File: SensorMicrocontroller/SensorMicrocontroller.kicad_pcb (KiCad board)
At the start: 2 copper layers, 100 x 100 mm, 36 parts, among them J1 JST B4B-PH-SM4-TB, J2 JST B4B-PH-SM4-TB, J3 JST B6B-PH-SM4-TB, J4 JST B4B-PH-SM4-TB, J5 JST B4B-PH-SM4-TB, J8 12V Connector, J9 Light Connector, Q1 DMT6009LCT, Q2 DMT6009LCT, U1 ADS1115IDGS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

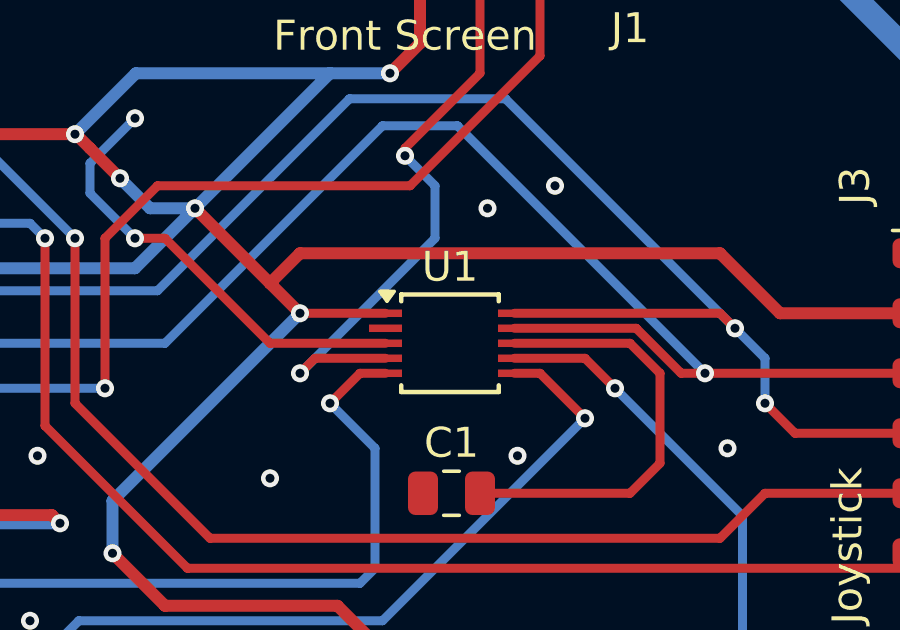
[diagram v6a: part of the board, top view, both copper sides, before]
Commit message: Fixed ADS1115 footprint
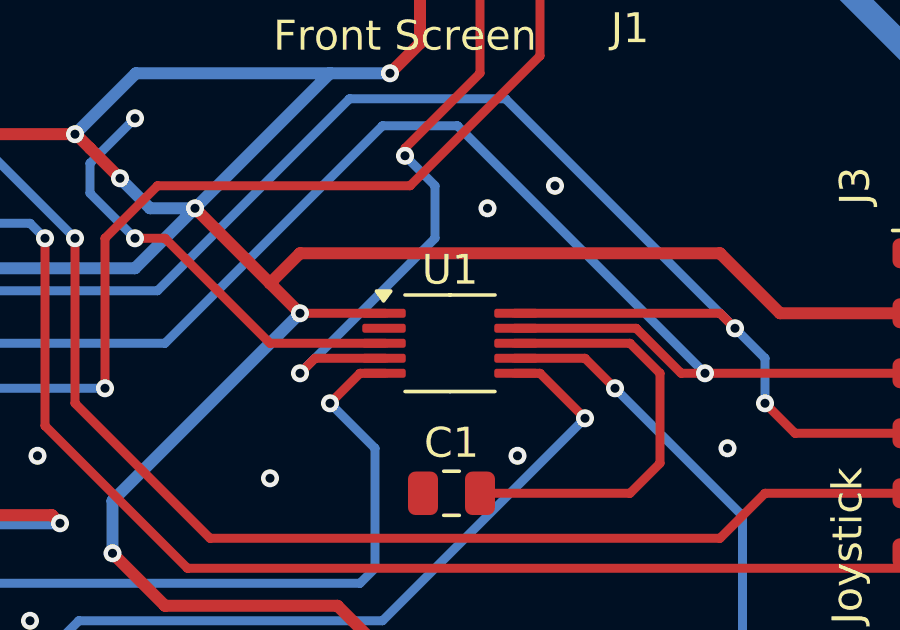
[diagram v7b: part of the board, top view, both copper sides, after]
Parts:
- U1: footprint Package_SO:TSSOP-10_3x3mm_P0.5mm -> Package_SO:VSSOP-10_3x3mm_P0.5mm
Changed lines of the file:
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@@
 		)
 	)
-	(footprint "Package_SO:TSSOP-10_3x3mm_P0.5mm"
+	(footprint "Package_SO:VSSOP-10_3x3mm_P0.5mm"
 		(layer "F.Cu")
 		(at 172 68)
-		(descr "TSSOP10: plastic thin shrink small outline package; 10 leads; body width 3 mm; (see NXP SSOP-TSSOP-VSO-REFLOW.pdf and sot552-1_po.pdf)")
-		(tags "SSOP 0.5")
+		(descr "VSSOP, 10 Pin (http://www.ti.com/lit/ds/symlink/ads1115.pdf), generated with kicad-footprint-generator ipc_gullwing_generator.py")
+		(tags "VSSOP SO")
 		(property "Reference" "U1"
-			(at 0 -2.55 0)
+			(at 0 -2.45 0)
 			(layer "F.SilkS")
 			(effects
@@
 		)
 		(property "Value" "ADS1115IDGS"
-			(at 0 2.55 0)
+			(at 0 2.45 0)
 			(layer "F.Fab")
 			(effects
@@
 			)
 		)
-		(property "Footprint" "Package_SO:TSSOP-10_3x3mm_P0.5mm"
-			(at 0 0 0)
-			(unlocked yes)
+		(property "Footprint" "Package_SO:VSSOP-10_3x3mm_P0.5mm"
+			(at 0 0 0)
 			(layer "F.Fab")
 			(hide yes)
@@
 		(property "Datasheet" "http://www.ti.com/lit/ds/symlink/ads1113.pdf"
 			(at 0 0 0)
-			(unlocked yes)
 			(layer "F.Fab")
 			(hide yes)
@@
 		(property "Description" "Ultra-Small, Low-Power, I2C-Compatible, 860-SPS, 16-Bit ADCs With Internal Reference, Oscillator, and Programmable Comparator, VSSOP-10"
 			(at 0 0 0)
-			(unlocked yes)
 			(layer "F.Fab")
 			(hide yes)
@@
 		(attr smd)
 		(fp_line
-			(start -1.625 -1.625)
-			(end -1.625 -1.4)
-			(stroke
-				(width 0.15)
-				(type solid)
-			)
-			(layer "F.SilkS")
-		)
-		(fp_line
-			(start -1.625 -1.625)
-			(end 1.625 -1.625)
-			(stroke
-				(width 0.15)
-				(type solid)
-			)
-			(layer "F.SilkS")
-		)
-		(fp_line
-			(start -1.625 1.625)
-			(end -1.625 1.4)
-			(stroke
-				(width 0.15)
-				(type solid)
-			)
-			(layer "F.SilkS")
-		)
-		(fp_line
-			(start -1.625 1.625)
-			(end 1.625 1.625)
-			(stroke
-				(width 0.15)
-				(type solid)
-			)
-			(layer "F.SilkS")
-		)
-		(fp_line
-			(start 1.625 -1.625)
-			(end 1.625 -1.4)
-			(stroke
-				(width 0.15)
-				(type solid)
-			)
-			(layer "F.SilkS")
-		)
-		(fp_line
-			(start 1.625 1.625)
-			(end 1.625 1.4)
-			(stroke
-				(width 0.15)
+			(start 0 -1.61)
+			(end -1.5 -1.61)
+			(stroke
+				(width 0.12)
+				(type solid)
+			)
+			(layer "F.SilkS")
+		)
+		(fp_line
+			(start 0 -1.61)
+			(end 1.5 -1.61)
+			(stroke
+				(width 0.12)
+				(type solid)
+			)
+			(layer "F.SilkS")
+		)
+		(fp_line
+			(start 0 1.61)
+			(end -1.5 1.61)
+			(stroke
+				(width 0.12)
+				(type solid)
+			)
+			(layer "F.SilkS")
+		)
+		(fp_line
+			(start 0 1.61)
+			(end 1.5 1.61)
+			(stroke
+				(width 0.12)
 				(type solid)
 			)
@@
 		(fp_poly
 			(pts
-				(xy -2.1 -1.4) (xy -2.34 -1.73) (xy -1.86 -1.73) (xy -2.1 -1.4)
+				(xy -2.2125 -1.41) (xy -2.4525 -1.74) (xy -1.9725 -1.74) (xy -2.2125 -1.41)
 			)
 			(stroke
@@
 		)
 		(fp_line
-			(start -2.95 -1.8)
-			(end -2.95 1.8)
+			(start -3.18 -1.75)
+			(end -3.18 1.75)
 			(stroke
 				(width 0.05)
@@
 		)
 		(fp_line
-			(start -2.95 -1.8)
-			(end 2.95 -1.8)
+			(start -3.18 1.75)
+			(end 3.18 1.75)
 			(stroke
 				(width 0.05)
@@
 		)
 		(fp_line
-			(start -2.95 1.8)
-			(end 2.95 1.8)
+			(start 3.18 -1.75)
+			(end -3.18 -1.75)
 			(stroke
 				(width 0.05)
@@
 		)
 		(fp_line
-			(start 2.95 -1.8)
-			(end 2.95 1.8)
+			(start 3.18 1.75)
+			(end 3.18 -1.75)
 			(stroke
 				(width 0.05)
@@
 		)
 		(fp_line
-			(start -1.5 -0.5)
-			(end -0.5 -1.5)
+			(start -1.5 -0.75)
+			(end -0.75 -1.5)
 			(stroke
 				(width 0.1)
@@
 		(fp_line
 			(start -1.5 1.5)
-			(end -1.5 -0.5)
-			(stroke
-				(width 0.1)
-				(type solid)
-			)
-			(layer "F.Fab")
-		)
-		(fp_line
-			(start -0.5 -1.5)
+			(end -1.5 -0.75)
+			(stroke
+				(width 0.1)
+				(type solid)
+			)
+			(layer "F.Fab")
+		)
+		(fp_line
+			(start -0.75 -1.5)
 			(end 1.5 -1.5)
 			(stroke
@@
 			(effects
 				(font
-					(size 0.6 0.6)
-					(thickness 0.1)
-				)
-			)
-		)
-		(pad "1" smd rect
-			(at -2.15 -1)
-			(size 1.1 0.25)
-			(layers "F.Cu" "F.Paste" "F.Mask")
+					(size 0.75 0.75)
+					(thickness 0.11)
+				)
+			)
+		)
+		(pad "1" smd roundrect
+			(at -2.2 -1)
+			(size 1.45 0.3)
+			(layers "F.Cu" "F.Paste" "F.Mask")
+			(roundrect_rratio 0.25)
 			(net 7 "/3.3V")
 			(pinfunction "ADDR")
 			(pintype "input")
 		)
-		(pad "2" smd rect
-			(at -2.15 -0.5)
-			(size 1.1 0.25)
-			(layers "F.Cu" "F.Paste" "F.Mask")
+		(pad "2" smd roundrect
+			(at -2.2 -0.5)
+			(size 1.45 0.3)
+			(layers "F.Cu" "F.Paste" "F.Mask")
+			(roundrect_rratio 0.25)
 			(net 29 "unconnected-(U1-ALERT{slash}RDY-Pad2)")
 			(pinfunction "ALERT/RDY")
 			(pintype "output")
 		)
-		(pad "3" smd rect
-			(at -2.15 0)
-			(size 1.1 0.25)
-			(layers "F.Cu" "F.Paste" "F.Mask")
+		(pad "3" smd roundrect
+			(at -2.2 0)
+			(size 1.45 0.3)
+			(layers "F.Cu" "F.Paste" "F.Mask")
+			(roundrect_rratio 0.25)
 			(net 2 "/GND")
 			(pinfunction "GND")
 			(pintype "power_in")
 		)
-		(pad "4" smd rect
-			(at -2.15 0.5)
-			(size 1.1 0.25)
-			(layers "F.Cu" "F.Paste" "F.Mask")
+		(pad "4" smd roundrect
+			(at -2.2 0.5)
+			(size 1.45 0.3)
+			(layers "F.Cu" "F.Paste" "F.Mask")
+			(roundrect_rratio 0.25)
 			(net 9 "/US0")
 			(pinfunction "AIN0")
 			(pintype "input")
 		)
-		(pad "5" smd rect
-			(at -2.15 1)
-			(size 1.1 0.25)
-			(layers "F.Cu" "F.Paste" "F.Mask")
+		(pad "5" smd roundrect
+			(at -2.2 1)
+			(size 1.45 0.3)
+			(layers "F.Cu" "F.Paste" "F.Mask")
+			(roundrect_rratio 0.25)
 			(net 11 "/US1")
 			(pinfunction "AIN1")
 			(pintype "input")
 		)
-		(pad "6" smd rect
-			(at 2.15 1)
-			(size 1.1 0.25)
-			(layers "F.Cu" "F.Paste" "F.Mask")
+		(pad "6" smd roundrect
+			(at 2.2 1)
+			(size 1.45 0.3)
+			(layers "F.Cu" "F.Paste" "F.Mask")
+			(roundrect_rratio 0.25)
 			(net 12 "/US2")
 			(pinfunction "AIN2")
 			(pintype "input")
 		)
-		(pad "7" smd rect
-			(at 2.15 0.5)
-			(size 1.1 0.25)
-			(layers "F.Cu" "F.Paste" "F.Mask")
+		(pad "7" smd roundrect
+			(at 2.2 0.5)
+			(size 1.45 0.3)
+			(layers "F.Cu" "F.Paste" "F.Mask")
+			(roundrect_rratio 0.25)
 			(net 14 "/US3")
 			(pinfunction "AIN3")
 			(pintype "input")
 		)
-		(pad "8" smd rect
-			(at 2.15 0)
-			(size 1.1 0.25)
-			(layers "F.Cu" "F.Paste" "F.Mask")
+		(pad "8" smd roundrect
+			(at 2.2 0)
+			(size 1.45 0.3)
+			(layers "F.Cu" "F.Paste" "F.Mask")
+			(roundrect_rratio 0.25)
 			(net 1 "Net-(U1-VDD)")
 			(pinfunction "VDD")
 			(pintype "power_in")
 		)
-		(pad "9" smd rect
-			(at 2.15 -0.5)
-			(size 1.1 0.25)
-			(layers "F.Cu" "F.Paste" "F.Mask")
+		(pad "9" smd roundrect
+			(at 2.2 -0.5)
+			(size 1.45 0.3)
+			(layers "F.Cu" "F.Paste" "F.Mask")
+			(roundrect_rratio 0.25)
 			(net 6 "/SDA")
 			(pinfunction "SDA")
 			(pintype "bidirectional")
 		)
-		(pad "10" smd rect
-			(at 2.15 -1)
-			(size 1.1 0.25)
-			(layers "F.Cu" "F.Paste" "F.Mask")
+		(pad "10" smd roundrect
+			(at 2.2 -1)
+			(size 1.45 0.3)
+			(layers "F.Cu" "F.Paste" "F.Mask")
+			(roundrect_rratio 0.25)
 			(net 4 "/SCL")
 			(pinfunction "SCL")
 			(pintype "input")
 		)
-		(model "${KICAD8_3DMODEL_DIR}/Package_SO.3dshapes/TSSOP-10_3x3mm_P0.5mm.wrl"
+		(model "${KICAD8_3DMODEL_DIR}/Package_SO.3dshapes/VSSOP-10_3x3mm_P0.5mm.wrl"
 			(offset
 				(xyz 0 0 0)

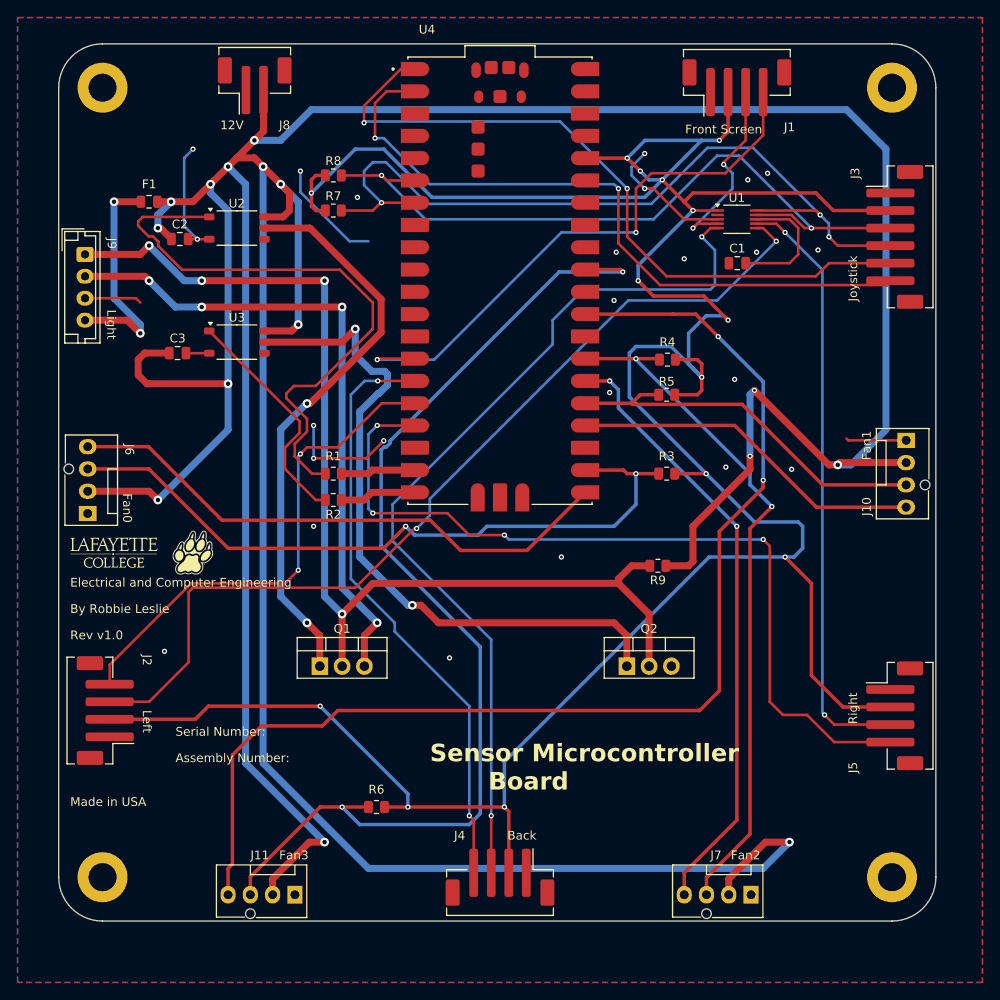
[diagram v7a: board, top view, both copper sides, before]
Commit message: Added cap for fan tach
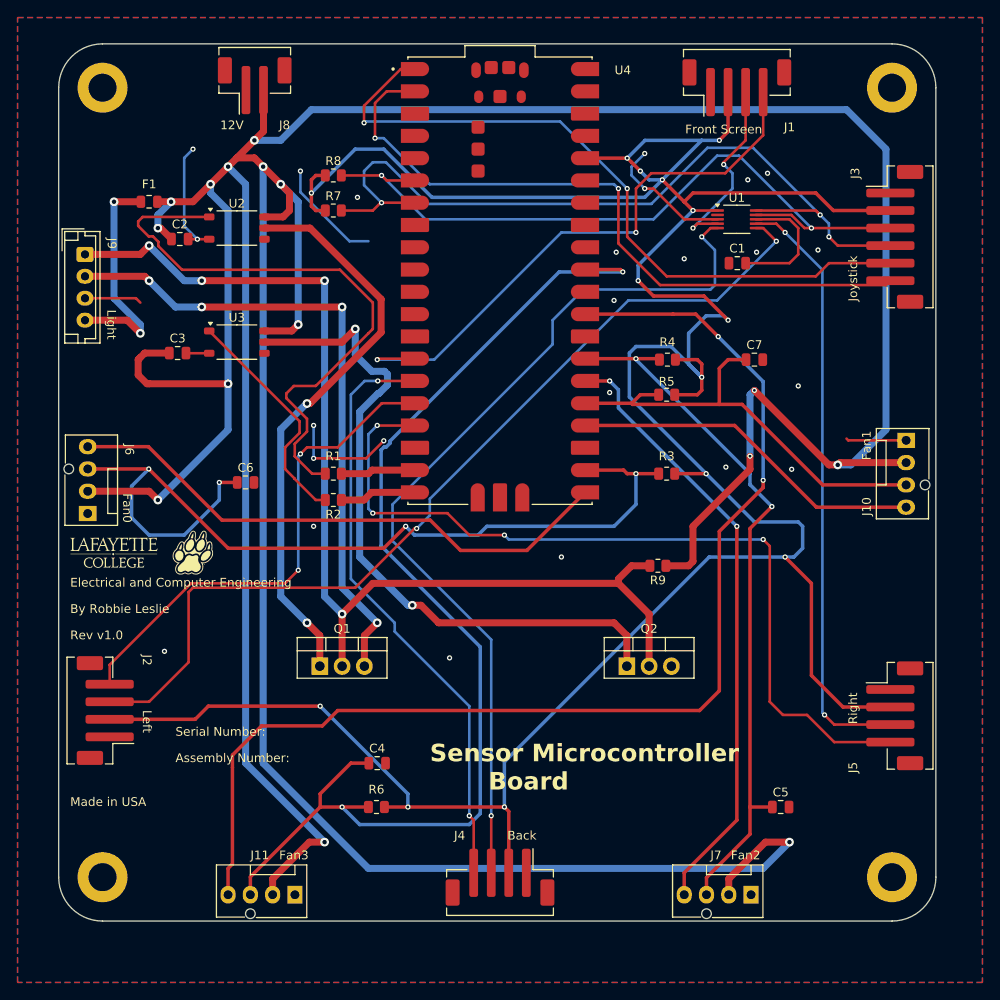
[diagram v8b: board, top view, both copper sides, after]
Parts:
- added C4: 1nF, Capacitor_SMD:C_0805_2012Metric, F.Cu at (131.0, 130.0)
- added C5: 1nF, Capacitor_SMD:C_0805_2012Metric, F.Cu at (177.0, 135.0)
- added C6: 1nF, Capacitor_SMD:C_0805_2012Metric, F.Cu at (116.0, 98.0)
- added C7: 1nF, Capacitor_SMD:C_0805_2012Metric, F.Cu at (174.0, 84.0)
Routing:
- net /Fan Sense0: track 81.2 -> 104.1 mm, vias 2 -> 4
- net /Fan Sense3: track 122.5 -> 131.0 mm
- net /Fan Sense1: track 44.0 -> 51.5 mm
- net /Fan Sense2: track 79.0 -> 81.6 mm
